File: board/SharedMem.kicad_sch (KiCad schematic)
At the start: 10 parts, among them U19 628512_DIP32, U20 628512_DIP32, U21 628512_DIP32, U22 628512_DIP32, U23 74LS139

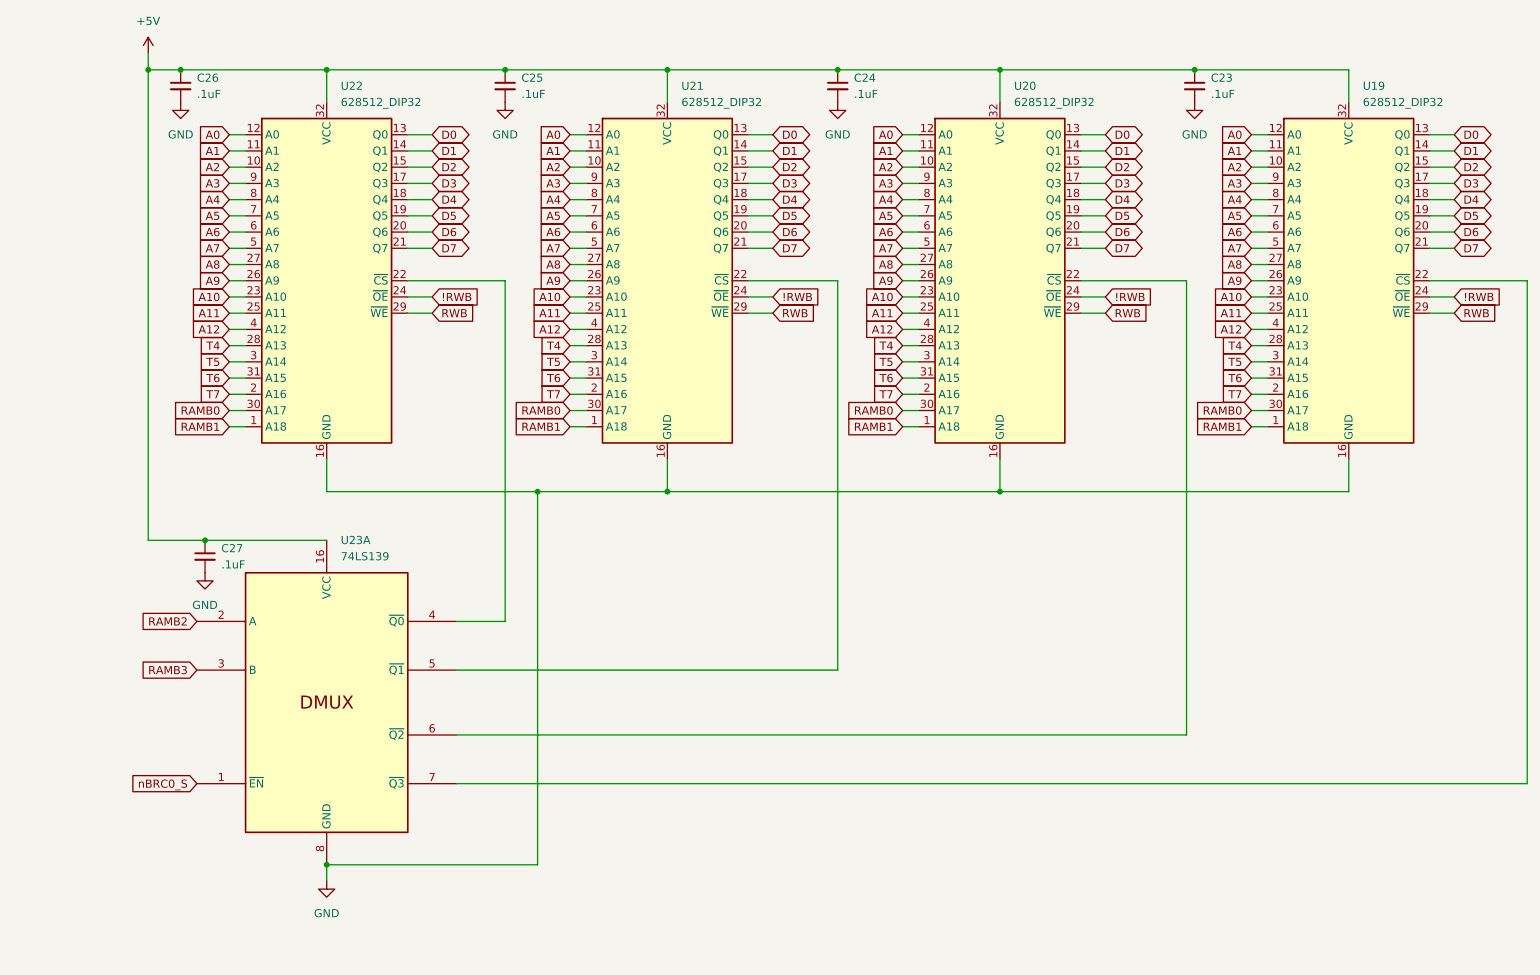
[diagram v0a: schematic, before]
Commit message: Fixing pin assignments
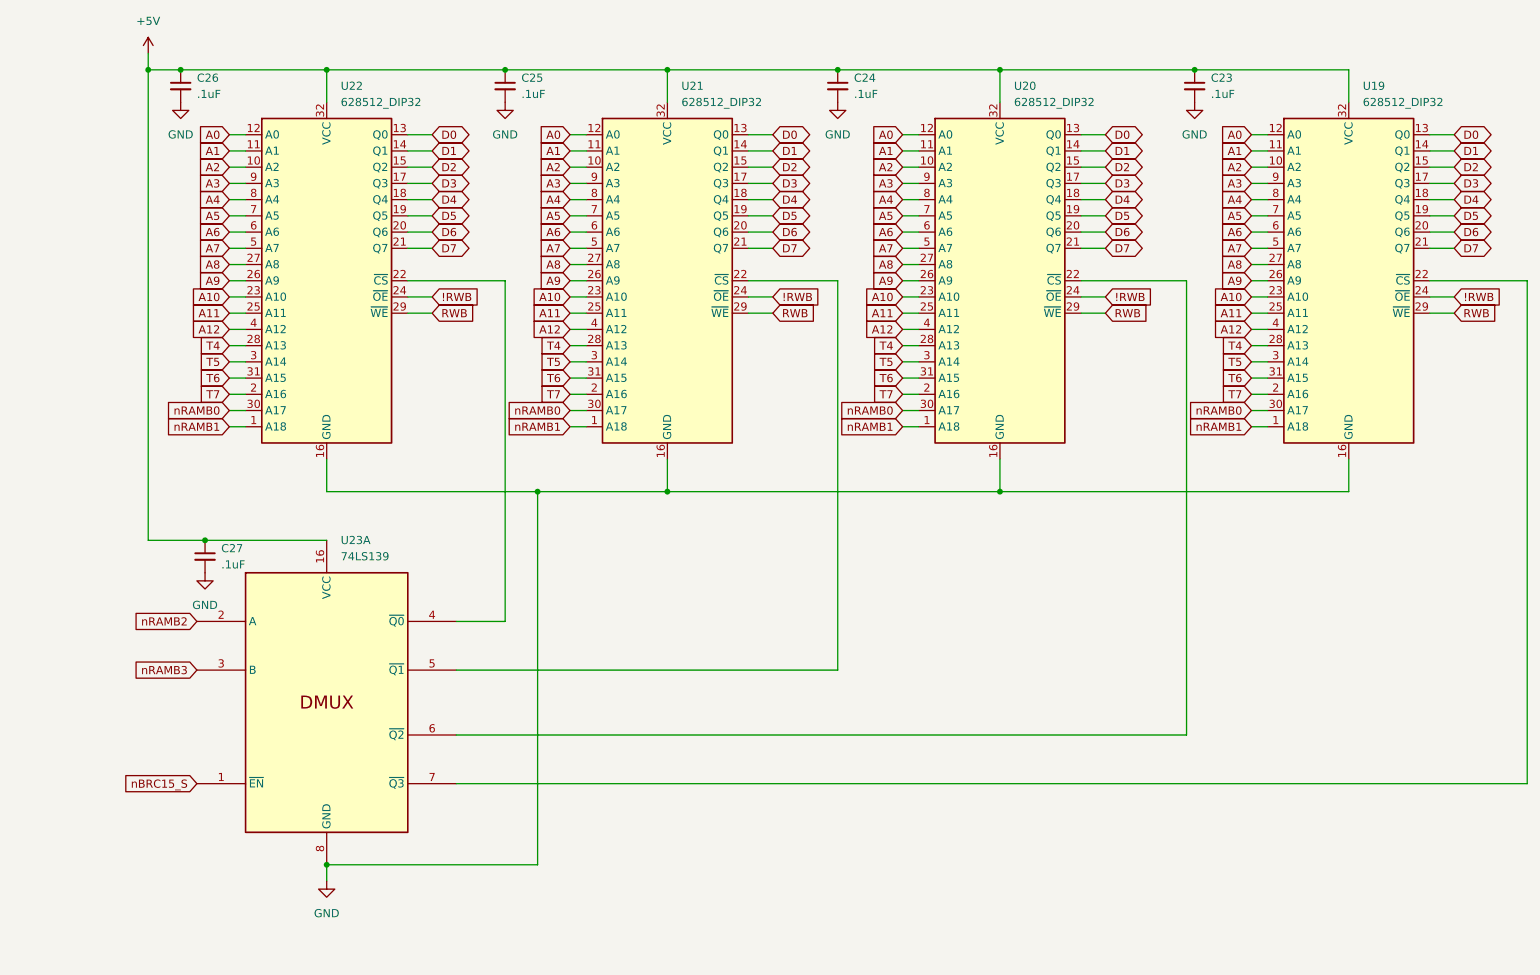
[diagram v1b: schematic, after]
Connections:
- net RAMB0 renamed nRAMB0
- net RAMB1 renamed nRAMB1
- net RAMB2 renamed nRAMB2
- net RAMB3 renamed nRAMB3
- net nBRC0_S renamed nBRC15_S
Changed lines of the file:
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@@
 		)
 	)
-	(global_label "RAMB3"
+	(global_label "nRAMB3"
 		(shape input)
 		(at 45.72 124.46 180)
@@
 		)
 		(property "Intersheetrefs" "${INTERSHEET_REFS}"
-			(at 36.4453 124.46 0)
-			(effects
-				(font
-					(size 1.27 1.27)
-				)
-				(justify right)
-				(hide yes)
-			)
-		)
-	)
-	(global_label "RAMB1"
+			(at 35.2963 124.46 0)
+			(effects
+				(font
+					(size 1.27 1.27)
+				)
+				(justify right)
+				(hide yes)
+			)
+		)
+	)
+	(global_label "nRAMB1"
 		(shape input)
 		(at 104.14 86.36 180)
@@
 		)
 		(property "Intersheetrefs" "${INTERSHEET_REFS}"
-			(at 94.8653 86.36 0)
+			(at 93.7163 86.36 0)
 			(effects
 				(font
@@
 		)
 	)
-	(global_label "RAMB0"
+	(global_label "nRAMB0"
 		(shape input)
 		(at 104.14 83.82 180)
@@
 		)
 		(property "Intersheetrefs" "${INTERSHEET_REFS}"
-			(at 94.8653 83.82 0)
+			(at 93.7163 83.82 0)
 			(effects
 				(font
@@
 		)
 	)
-	(global_label "RAMB0"
+	(global_label "nRAMB0"
 		(shape input)
 		(at 50.8 83.82 180)
@@
 		)
 		(property "Intersheetrefs" "${INTERSHEET_REFS}"
-			(at 41.5253 83.82 0)
+			(at 40.3763 83.82 0)
 			(effects
 				(font
@@
 		)
 	)
-	(global_label "RAMB1"
+	(global_label "nRAMB1"
 		(shape input)
 		(at 210.82 86.36 180)
@@
 		)
 		(property "Intersheetrefs" "${INTERSHEET_REFS}"
-			(at 201.5453 86.36 0)
+			(at 200.3963 86.36 0)
 			(effects
 				(font
@@
 		)
 	)
-	(global_label "RAMB0"
+	(global_label "nRAMB0"
 		(shape input)
 		(at 210.82 83.82 180)
@@
 		)
 		(property "Intersheetrefs" "${INTERSHEET_REFS}"
-			(at 201.5453 83.82 0)
+			(at 200.3963 83.82 0)
 			(effects
 				(font
@@
 		)
 	)
-	(global_label "RAMB2"
+	(global_label "nRAMB2"
 		(shape input)
 		(at 45.72 116.84 180)
@@
 		)
 		(property "Intersheetrefs" "${INTERSHEET_REFS}"
-			(at 36.4453 116.84 0)
+			(at 35.2963 116.84 0)
 			(effects
 				(font
@@
 		)
 	)
-	(global_label "RAMB1"
+	(global_label "nRAMB1"
 		(shape input)
 		(at 50.8 86.36 180)
@@
 		)
 		(property "Intersheetrefs" "${INTERSHEET_REFS}"
-			(at 41.5253 86.36 0)
+			(at 40.3763 86.36 0)
 			(effects
 				(font
@@
 		)
 	)
-	(global_label "RAMB1"
+	(global_label "nRAMB1"
 		(shape input)
 		(at 156.21 86.36 180)
@@
 		)
 		(property "Intersheetrefs" "${INTERSHEET_REFS}"
-			(at 146.9353 86.36 0)
+			(at 145.7863 86.36 0)
 			(effects
 				(font
@@
 		)
 	)
-	(global_label "nBRC0_S"
+	(global_label "nBRC15_S"
 		(shape input)
 		(at 45.72 142.24 180)
@@
 		)
 		(property "Intersheetrefs" "${INTERSHEET_REFS}"
-			(at 34.3892 142.24 0)
+			(at 33.1797 142.24 0)
 			(effects
 				(font
@@
 		)
 	)
-	(global_label "RAMB0"
+	(global_label "nRAMB0"
 		(shape input)
 		(at 156.21 83.82 180)
@@
 		)
 		(property "Intersheetrefs" "${INTERSHEET_REFS}"
-			(at 146.9353 83.82 0)
-			(effects
-				(font
+			(at 145.7863 83.82 0)
+			(effects
+				(font

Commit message: Added surface mount version of memory daughter cards, and lots of schematic updates and fixes, including adding dedicated registers for shared memory bank select at $FFF1 and IRQ vTable entry selector at $FFF2 along with the IRQ vTable registers and priority encoders for 16 IRQs
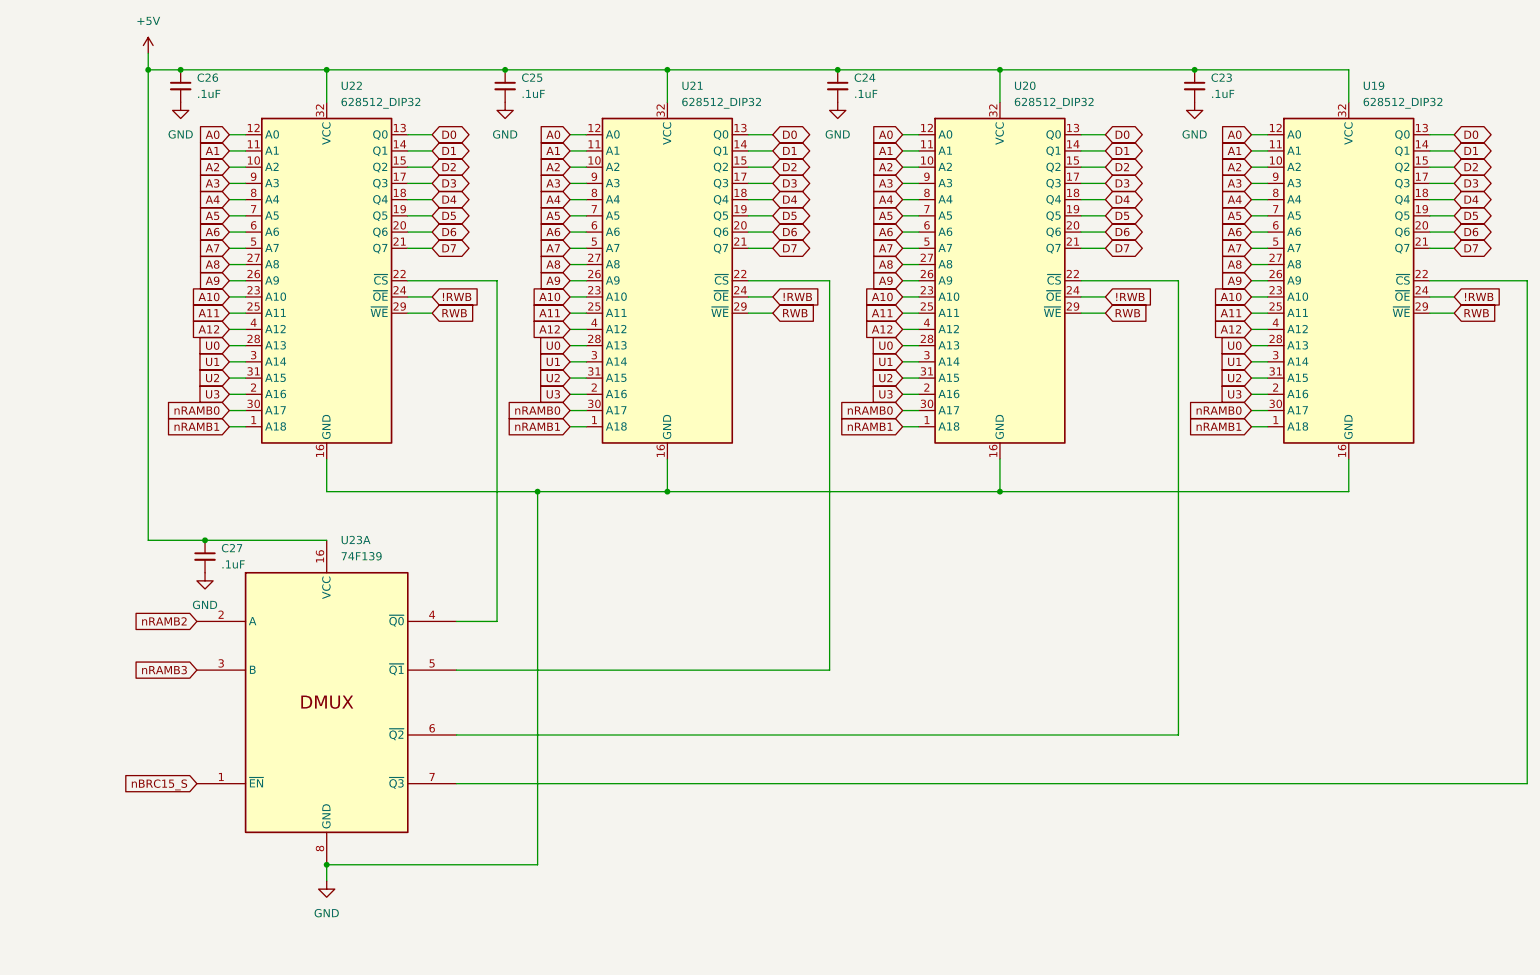
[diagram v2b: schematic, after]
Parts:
- U23: value 74LS139 -> 74F139
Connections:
- net T4 renamed U0
- net T5 renamed U1
- net T6 renamed U2
- net T7 renamed U3

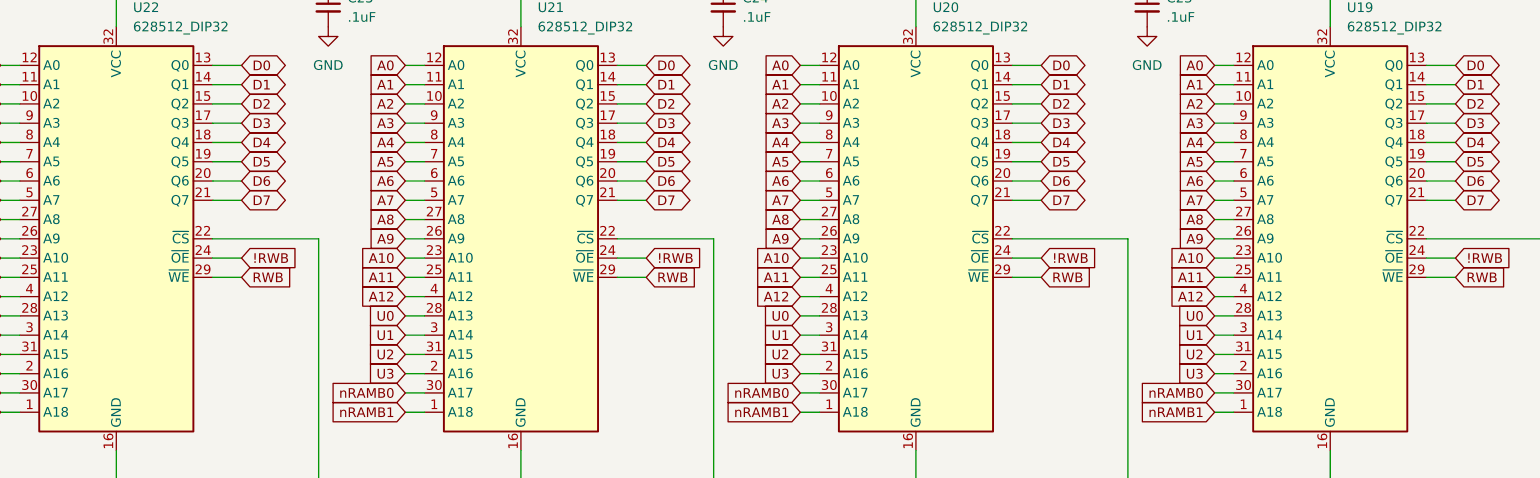
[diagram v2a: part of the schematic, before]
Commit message: More main PCB updates.  Rearranged some things.  Bypass caps near PS connector.  Moved front panel connector to opposite side of board.
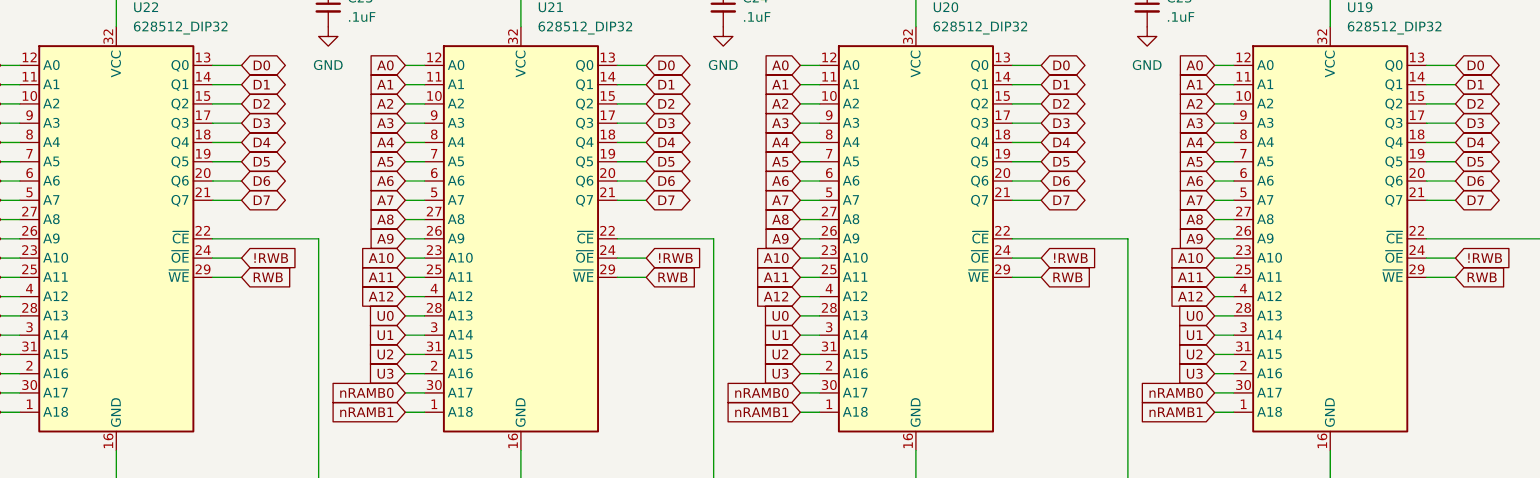
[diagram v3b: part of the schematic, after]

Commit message: Latest main PCB update with FFF1 and FFF2 added and decode logic updated to exclude FFFE and FFFF in nOSROM_S signal
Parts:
- U23: footprint Package_DIP:DIP-16_W7.62mm_LongPads -> Package_DIP:DIP-16_W7.62mm_Socket_LongPads
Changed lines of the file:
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@@
 			)
 		)
-		(property "Footprint" "Package_DIP:DIP-16_W7.62mm_LongPads"
+		(property "Footprint" "Package_DIP:DIP-16_W7.62mm_Socket_LongPads"
 			(at 66.04 129.54 0)
 			(effects

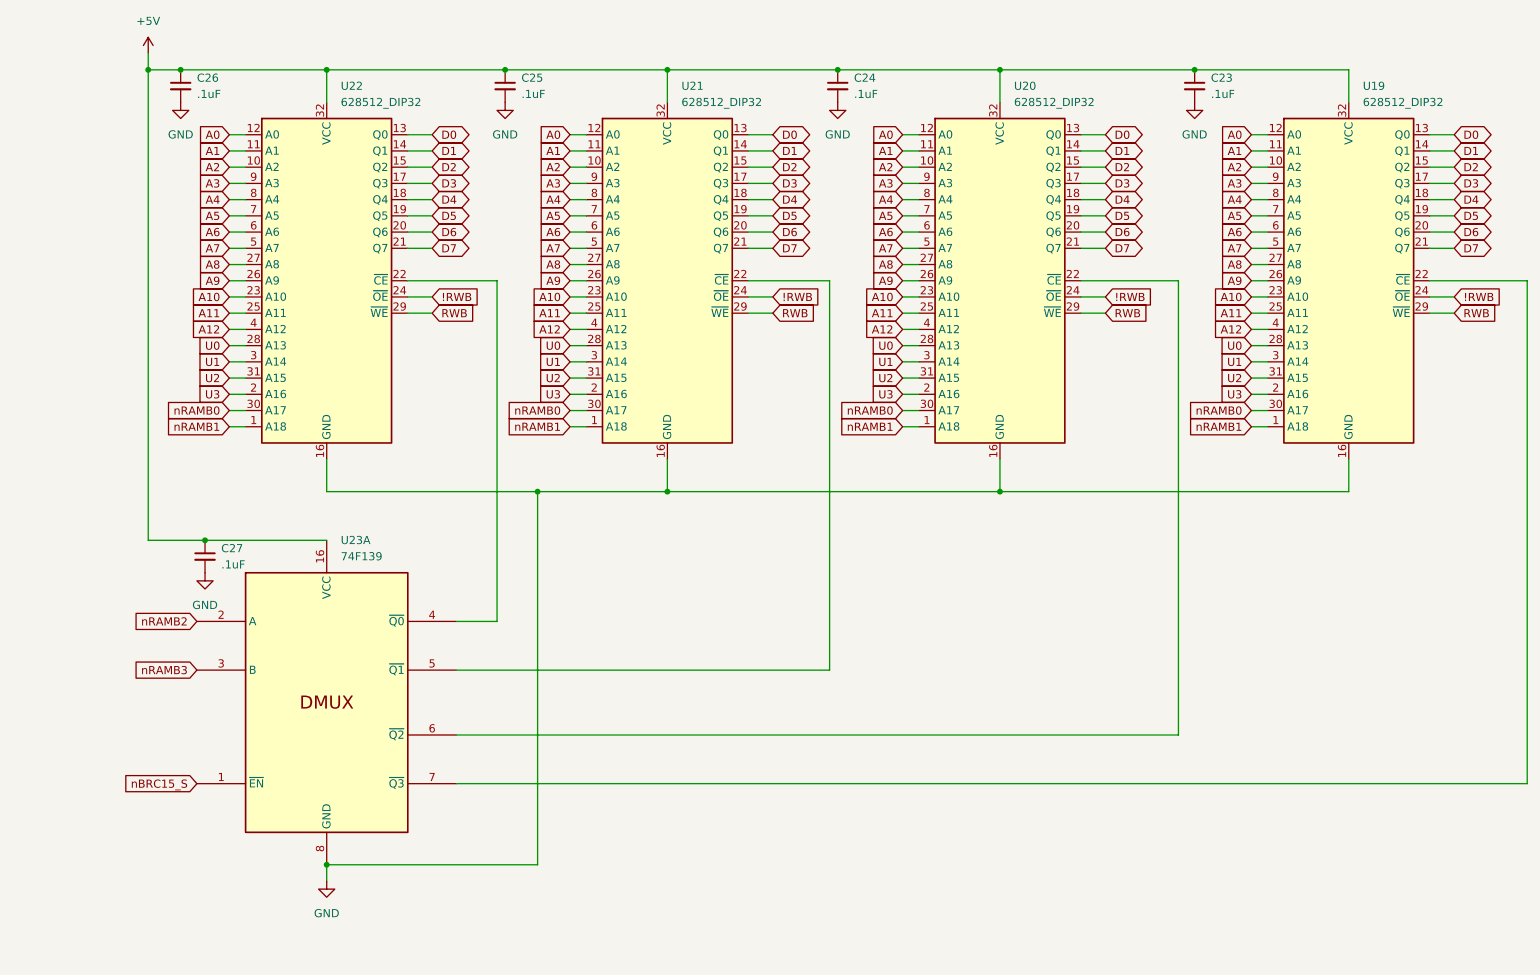
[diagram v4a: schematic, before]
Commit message: Schematic Bus updates, silkscreen updates, position tweaks, and other corrections.
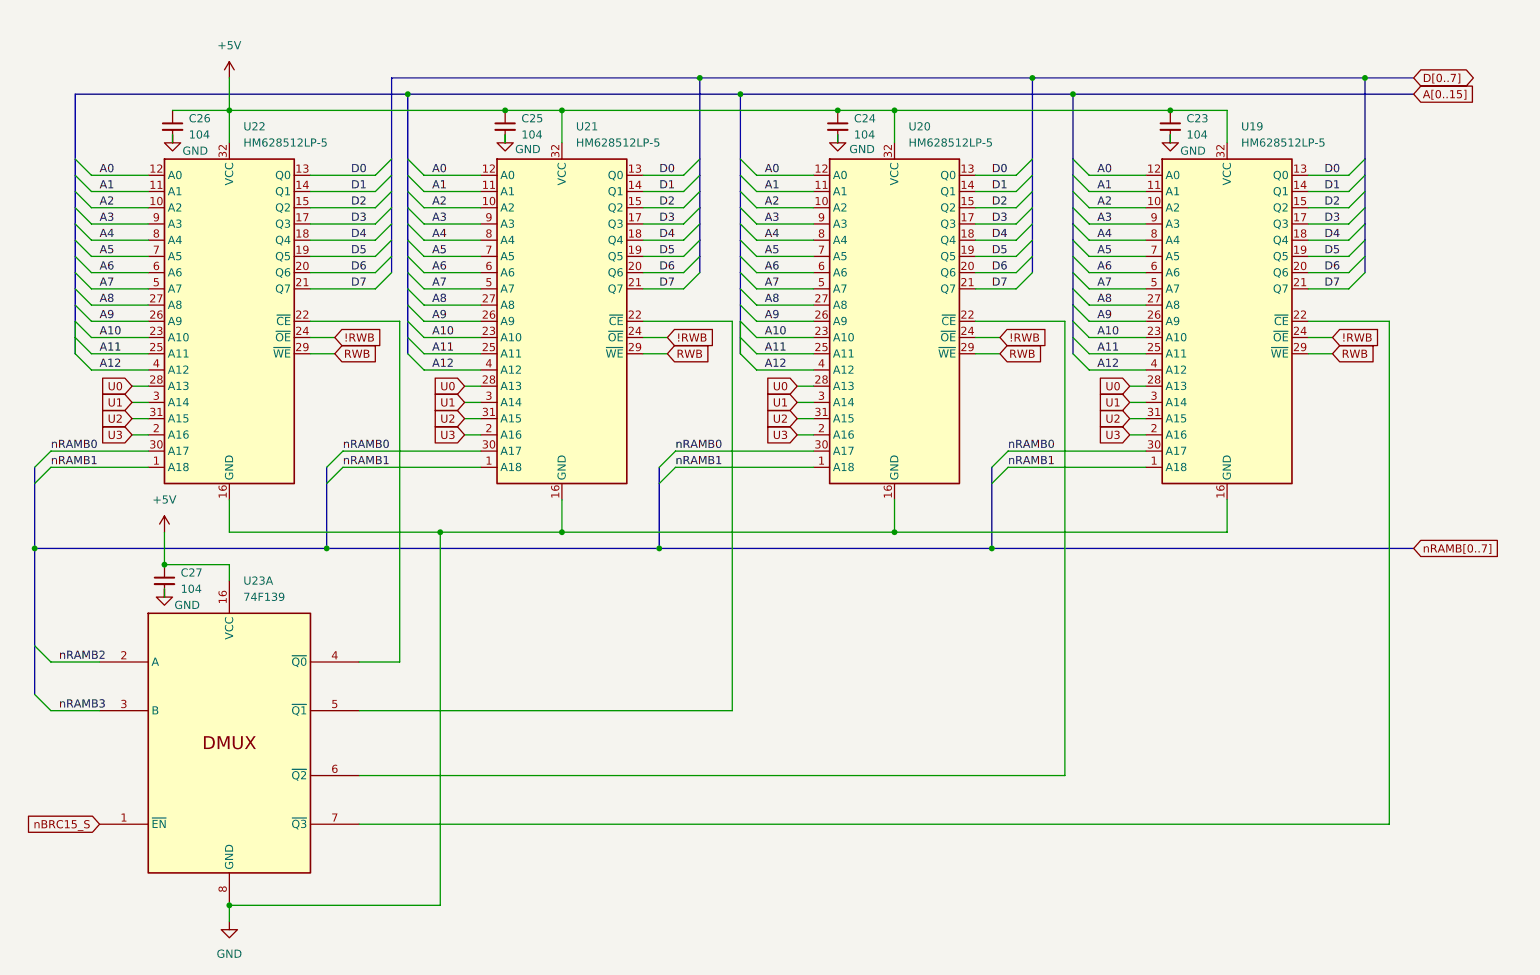
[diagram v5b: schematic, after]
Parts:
- C23, C24, C25, C26, C27: value .1uF -> 104
- U19, U20, U21, U22: value 628512_DIP32 -> HM628512LP-5
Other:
- company: (none) -> Data Tuning
- title: (none) -> Shared RAM Banks
- moved on the sheet: C23, C24, C25, C26, C27, U19, U20, U21, U22, U23A
